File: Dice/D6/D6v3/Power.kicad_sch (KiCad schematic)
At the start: 20 parts, among them U4 LN3435, U6 MT9700, U7 74AHC1G08, U8 TMR1366

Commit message: Updating D8 and D10 boards, new antenna, etc...
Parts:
- W12, W18, W21, W23, W25: Generic OK (none) -> N/A
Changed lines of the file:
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@@
     )
     (property "Datasheet" "" (id 3) (at 185.42 139.7 0))
+    (property "Generic OK" "N/A" (id 4) (at 185.42 134.62 0)
+      (effects (font (size 1.27 1.27)) hide)
+    )
     (pin "1")
   )
@@
     )
     (property "Datasheet" "" (id 3) (at 147.32 54.61 0))
+    (property "Generic OK" "N/A" (id 4) (at 142.24 54.61 0)
+      (effects (font (size 1.27 1.27)) hide)
+    )
     (pin "1")
   )
@@
     )
     (property "Datasheet" "" (id 3) (at 87.63 96.52 0))
+    (property "Generic OK" "N/A" (id 4) (at 82.55 96.52 0)
+      (effects (font (size 1.27 1.27)) hide)
+    )
     (pin "1")
   )
@@
     )
     (property "Datasheet" "" (id 3) (at 205.74 111.76 0))
+    (property "Generic OK" "N/A" (id 4) (at 200.66 111.76 0)
+      (effects (font (size 1.27 1.27)) hide)
+    )
     (pin "1")
   )
@@
     )
     (property "Datasheet" "" (id 3) (at 214.63 58.42 0))
-    (pin "1")
-  )
+    (property "Generic OK" "N/A" (id 4) (at 214.63 53.34 0)
+      (effects (font (size 1.27 1.27)) hide)
+    )
+    (pin "1")
+  )

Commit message: Updates to D20V13, D6V3 and removing kicad_prl from git
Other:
- title: Pixels D20 Schematic, Power -> Pixels D6 Schematic, Main
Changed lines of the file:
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@@
   (paper "A4")
   (title_block
-    (title "Pixels D20 Schematic, Power")
-    (date "2020-04-13")
-    (rev "2")
+    (title "Pixels D6 Schematic, Main")
+    (date "2022-08-26")
+    (rev "3")
     (company "Systemic Games, LLC")
+    (comment 1 "Power Regulation")
   )
   (junction (at 142.24 62.23) (diameter 0) (color 0 0 0 0)

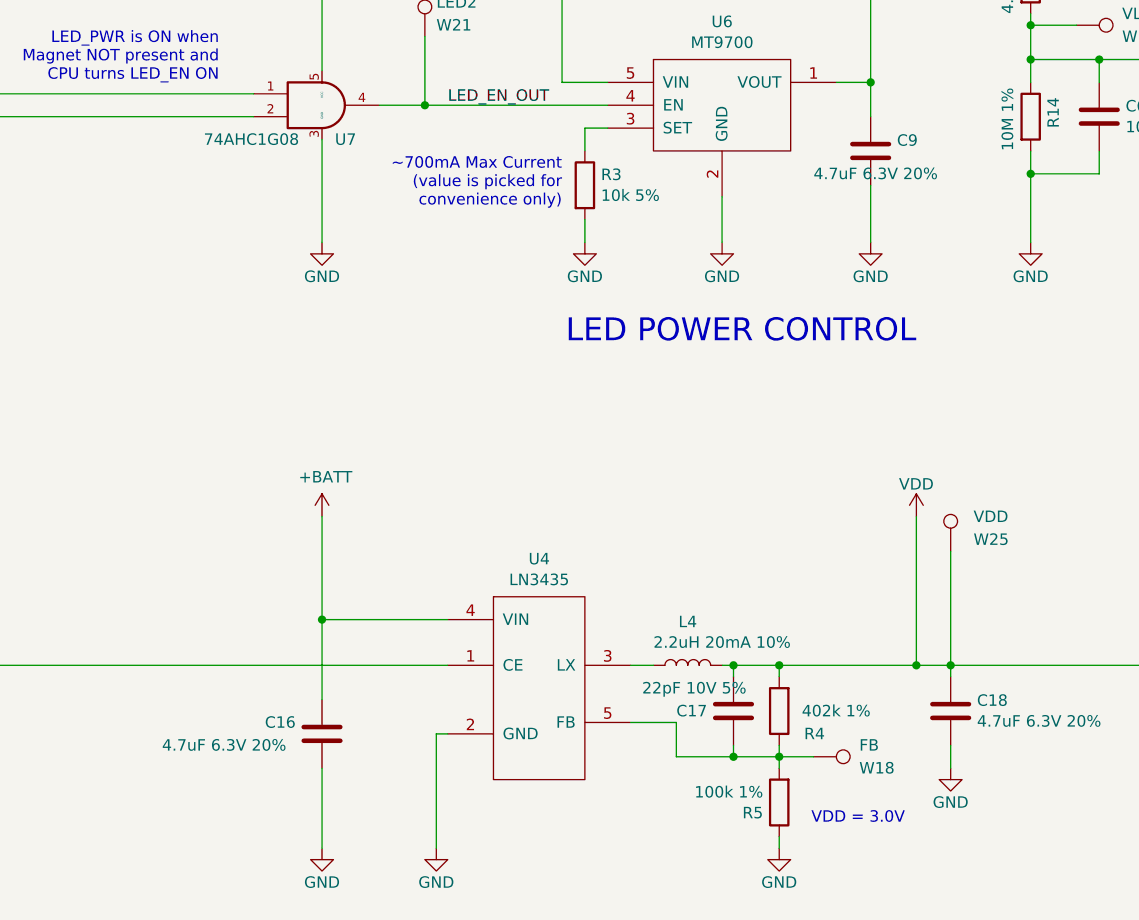
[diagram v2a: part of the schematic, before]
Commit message: Added D20V14, Update D6 to V3, PD6 to V2 and LCCV2
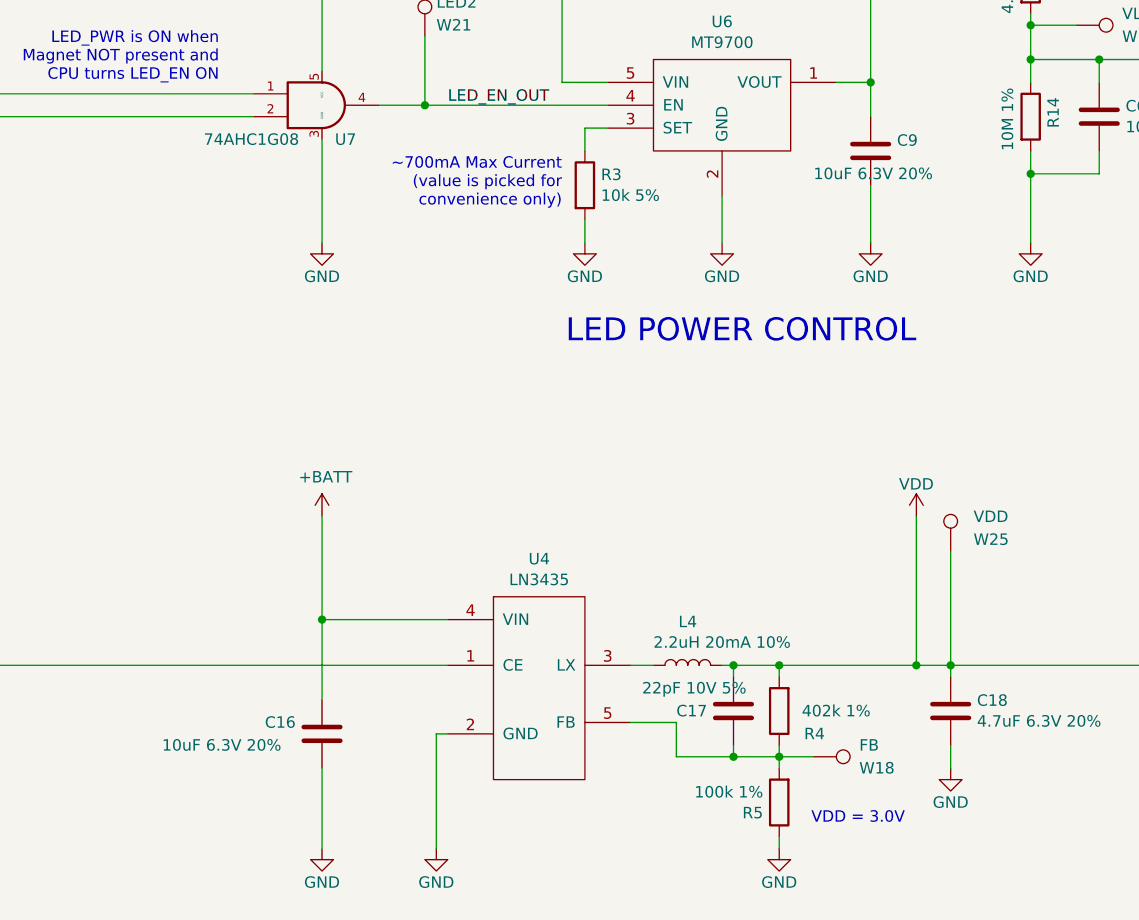
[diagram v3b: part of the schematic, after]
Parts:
- C16, C9: value 4.7uF 6.3V 20% -> 10uF 6.3V 20%; footprint Capacitor_SMD:C_0402_1005Metric -> Pixels-dice:C_0402_1005Metric; Manufacturer Part Number GRM155R60J475ME87D -> GRM155R60J106ME05J
- C17: Manufacturer Yageo -> Murata; Manufacturer Part Number CC0402JRNPO9BN220 -> GCM1555C1H220JA16J
- C6: Manufacturer Yageo -> Murata; Manufacturer Part Number AC0402KPX7R9BB103 -> GRM155R71H103KA88
- L4: Manufacturer Bourns -> Murata; Manufacturer Part Number CV201210-2R2K -> LQM21PN2R2MC0
- R13: Manufacturer Vishay -> UNI-ROYAL(Uniroyal Elec); Manufacturer Part Number CRCW04024M02FKED -> 0402WGF4024TCE
- R14: Manufacturer Yageo -> UNI-ROYAL(Uniroyal Elec); Manufacturer Part Number RC0402FR-0710ML -> 0402WGF1005TCE
- R3: Manufacturer Yageo -> UNI-ROYAL(Uniroyal Elec); Manufacturer Part Number RC0402JR-0710KL -> 0402WGJ0103TCE
- R4: Manufacturer Yageo -> UNI-ROYAL(Uniroyal Elec); Manufacturer Part Number RC0402FR-07402KL -> 0402WGF4023TCE
- R5: Manufacturer Vishay -> UNI-ROYAL(Uniroyal Elec); Manufacturer Part Number CRCW0402100KFKEDC -> 0402WGF1003TCE
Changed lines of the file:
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@@
       (effects (font (size 1.27 1.27)) hide)
     )
-    (property "Manufacturer" "Bourns" (id 6) (at 171.45 124.46 0)
-      (effects (font (size 1.27 1.27)) hide)
-    )
-    (property "Manufacturer Part Number" "CV201210-2R2K" (id 7) (at 171.45 124.46 0)
+    (property "Manufacturer" "Murata" (id 6) (at 171.45 124.46 0)
+      (effects (font (size 1.27 1.27)) hide)
+    )
+    (property "Manufacturer Part Number" "LQM21PN2R2MC0" (id 7) (at 171.45 124.46 0)
       (effects (font (size 1.27 1.27)) hide)
     )
@@
       (effects (font (size 1.27 1.27)) hide)
     )
-    (property "Manufacturer" "Yageo" (id 6) (at 176.53 129.54 0)
-      (effects (font (size 1.27 1.27)) hide)
-    )
-    (property "Manufacturer Part Number" "CC0402JRNPO9BN220" (id 7) (at 176.53 129.54 0)
+    (property "Manufacturer" "Murata" (id 6) (at 176.53 129.54 0)
+      (effects (font (size 1.27 1.27)) hide)
+    )
+    (property "Manufacturer Part Number" "GCM1555C1H220JA16J" (id 7) (at 176.53 129.54 0)
       (effects (font (size 1.27 1.27)) hide)
     )
@@
       (effects (font (size 1.27 1.27)) hide)
     )
-    (property "Manufacturer" "Vishay" (id 6) (at 181.61 139.7 0)
-      (effects (font (size 1.27 1.27)) hide)
-    )
-    (property "Manufacturer Part Number" "CRCW0402100KFKEDC" (id 7) (at 181.61 139.7 0)
+    (property "Manufacturer" "UNI-ROYAL(Uniroyal Elec)" (id 6) (at 181.61 139.7 0)
+      (effects (font (size 1.27 1.27)) hide)
+    )
+    (property "Manufacturer Part Number" "0402WGF1003TCE" (id 7) (at 181.61 139.7 0)
       (effects (font (size 1.27 1.27)) hide)
     )
@@
       (effects (font (size 1.27 1.27)) hide)
     )
-    (property "Manufacturer" "Yageo" (id 6) (at 181.61 129.54 0)
-      (effects (font (size 1.27 1.27)) hide)
-    )
-    (property "Manufacturer Part Number" "RC0402FR-07402KL" (id 7) (at 181.61 129.54 0)
+    (property "Manufacturer" "UNI-ROYAL(Uniroyal Elec)" (id 6) (at 181.61 129.54 0)
+      (effects (font (size 1.27 1.27)) hide)
+    )
+    (property "Manufacturer Part Number" "0402WGF4023TCE" (id 7) (at 181.61 129.54 0)
       (effects (font (size 1.27 1.27)) hide)
     )
@@
       (effects (font (size 1.27 1.27)) (justify left))
     )
-    (property "Value" "4.7uF 6.3V 20%" (id 1) (at 113.03 133.35 0)
-      (effects (font (size 1.27 1.27)) (justify left))
-    )
-    (property "Footprint" "Capacitor_SMD:C_0402_1005Metric" (id 2) (at 131.7752 135.89 0)
+    (property "Value" "10uF 6.3V 20%" (id 1) (at 113.03 133.35 0)
+      (effects (font (size 1.27 1.27)) (justify left))
+    )
+    (property "Footprint" "Pixels-dice:C_0402_1005Metric" (id 2) (at 131.7752 135.89 0)
       (effects (font (size 1.27 1.27)) hide)
     )
@@
       (effects (font (size 1.27 1.27)) hide)
     )
-    (property "Manufacturer Part Number" "GRM155R60J475ME87D" (id 7) (at 130.81 132.08 0)
+    (property "Manufacturer Part Number" "GRM155R60J106ME05J" (id 7) (at 130.81 132.08 0)
       (effects (font (size 1.27 1.27)) hide)
     )
@@
       (effects (font (size 1.27 1.27)) hide)
     )
-    (property "Manufacturer" "Vishay" (id 6) (at 209.55 48.26 0)
-      (effects (font (size 1.27 1.27)) hide)
-    )
-    (property "Manufacturer Part Number" "CRCW04024M02FKED" (id 7) (at 209.55 48.26 0)
+    (property "Manufacturer" "UNI-ROYAL(Uniroyal Elec)" (id 6) (at 209.55 48.26 0)
+      (effects (font (size 1.27 1.27)) hide)
+    )
+    (property "Manufacturer Part Number" "0402WGF4024TCE" (id 7) (at 209.55 48.26 0)
       (effects (font (size 1.27 1.27)) hide)
     )
@@
       (effects (font (size 1.27 1.27)) hide)
     )
-    (property "Manufacturer" "Yageo" (id 6) (at 209.55 63.5 0)
-      (effects (font (size 1.27 1.27)) hide)
-    )
-    (property "Manufacturer Part Number" "RC0402FR-0710ML" (id 7) (at 209.55 63.5 0)
+    (property "Manufacturer" "UNI-ROYAL(Uniroyal Elec)" (id 6) (at 209.55 63.5 0)
+      (effects (font (size 1.27 1.27)) hide)
+    )
+    (property "Manufacturer Part Number" "0402WGF1005TCE" (id 7) (at 209.55 63.5 0)
       (effects (font (size 1.27 1.27)) hide)
     )
@@
       (effects (font (size 1.27 1.27)) hide)
     )
-    (property "Manufacturer" "Yageo" (id 6) (at 217.17 63.5 0)
-      (effects (font (size 1.27 1.27)) hide)
-    )
-    (property "Manufacturer Part Number" "AC0402KPX7R9BB103" (id 7) (at 217.17 63.5 0)
+    (property "Manufacturer" "Murata" (id 6) (at 217.17 63.5 0)
+      (effects (font (size 1.27 1.27)) hide)
+    )
+    (property "Manufacturer Part Number" "GRM155R71H103KA88" (id 7) (at 217.17 63.5 0)
       (effects (font (size 1.27 1.27)) hide)
     )
@@
       (effects (font (size 1.27 1.27)) (justify left))
     )
-    (property "Value" "4.7uF 6.3V 20%" (id 1) (at 185.42 69.85 0)
-      (effects (font (size 1.27 1.27)) (justify left))
-    )
-    (property "Footprint" "Capacitor_SMD:C_0402_1005Metric" (id 2) (at 192.7352 71.12 0)
+    (property "Value" "10uF 6.3V 20%" (id 1) (at 185.42 69.85 0)
+      (effects (font (size 1.27 1.27)) (justify left))
+    )
+    (property "Footprint" "Pixels-dice:C_0402_1005Metric" (id 2) (at 192.7352 71.12 0)
       (effects (font (size 1.27 1.27)) hide)
     )
@@
       (effects (font (size 1.27 1.27)) hide)
     )
-    (property "Manufacturer Part Number" "GRM155R60J475ME87D" (id 7) (at 191.77 67.31 0)
+    (property "Manufacturer Part Number" "GRM155R60J106ME05J" (id 7) (at 191.77 67.31 0)
       (effects (font (size 1.27 1.27)) hide)
     )
@@
       (effects (font (size 1.27 1.27)) hide)
     )
-    (property "Manufacturer" "Yageo" (id 5) (at 160.02 71.12 0)
-      (effects (font (size 1.27 1.27)) hide)
-    )
-    (property "Manufacturer Part Number" "RC0402JR-0710KL" (id 6) (at 160.02 71.12 0)
-      (effects (font (size 1.27 1.27)) hide)
-    )
+    (property "Manufacturer" "UNI-ROYAL(Uniroyal Elec)" (id 5) (at 160.02 71.12 0)
+      (effects (font (size 1.27 1.27)) hide)
+    )
+    (property "Manufacturer Part Number" "0402WGJ0103TCE" (id 6) (at 160.02 71.12 0)
+      (effects (font (size 1.27 1.27)) hide)
+    )
